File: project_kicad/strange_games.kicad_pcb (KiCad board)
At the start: 2 copper layers, 330 x 248.8 mm, 117 parts, among them J1 Display, M1 Motor_DC, Q1 Si2302A, Q3 Si2302A, Q4 Q_Photo, SW10 SW_Push, SW11 SW_Push, SW3 SW_Push, SW4 SW_Push, SW5 SW_Push, SW6 SW_Push, SW7 SW_Push, SW8 SW_Push, SW9 SW_Push, U1 charge controller, U2 boost converter, U3 LDL1117S33R, U4 ESP32-DEVKIT-V1, U5 TMP112xxDRL, U6 vibrating_sensor, U7 LSM6DS3, U8 MQ-135 gas sensor

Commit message: code changes
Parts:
- added C5: C_Generic, PCM_Capacitor_SMD_AKL:C_0402_1005Metric, F.Cu at (347.9, 47.6)
- added R19: 330_0805, PCM_4ms_Resistor:R_0805_2012Metric, F.Cu at (348.5, 42.1)
- added R27: 10k_0805, PCM_4ms_Resistor:R_0805_2012Metric, F.Cu at (348.5, 45.1)
- added SW1: SW_Push, Button_Switch_THT:SW_PUSH-12mm, F.Cu at (331.5, 44.9)
- added SW12: SW_Push, Button_Switch_THT:SW_PUSH-12mm, F.Cu at (331.5, 72.0)
- added SW2: SW_Push, Button_Switch_THT:SW_PUSH-12mm, F.Cu at (331.5, 58.5)

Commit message: pcb update
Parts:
- SW1, SW12, SW2: moved to B.Cu
- moved BT1 272.9 mm to (3.23, 10.3)
- moved SW1 184.7 mm to (146.8, 41.5), turned to -90 degrees
- moved C2 174.5 mm to (196.6, 50.6)
- moved Q4 174.5 mm to (203.2, 47.5)
- moved R20 174.5 mm to (200.6, 50.6)
- moved R28 174.5 mm to (198.6, 50.6)
- moved SW2 165.6 mm to (166.8, 41.5), turned to -90 degrees
- moved C5 160.3 mm to (187.6, 44.5), turned to 180 degrees
- moved R19 158.1 mm to (190.4, 44.5), turned to 180 degrees
- moved R27 158.1 mm to (190.4, 47.0)
- moved D3 151.9 mm to (155.2, 137.4), turned to 0 degrees
- moved SW12 147.9 mm to (186.8, 41.5), turned to -90 degrees
- moved L1 147.1 mm to (154.0, 141.2), turned to 90 degrees
- moved Q1 140.6 mm to (156.5, 145.3), turned to 90 degrees
- moved R15 140.1 mm to (153.1, 146.4), turned to 180 degrees
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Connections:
- J1 pad 23: SCL -> CLK
- U4 pad 12: B12 -> B8
- U4 pad 13: B6 -> B9
- U4 pad 17: B10 -> gas_signal
- U4 pad 18: B9 -> vibrating_signal
- U4 pad 19: open_box -> vibrating_motor
- U4 pad 20: vibrating_motor -> open_box
- U4 pad 21: B2 -> luminodiodes
- U4 pad 22: B1 -> B10
- U4 pad 23: B5 -> B11
- U4 pad 24: B4 -> B12
- U4 pad 25: B3 -> photo
- U4 pad 27: B11 -> A0_display
- U4 pad 3: A0_display -> B1
- U4 pad 4: luminodiodes -> B2
- U4 pad 5: vibrating_signal -> B3
- U4 pad 6: B8 -> B4
- U4 pad 7: B7 -> B5
- U4 pad 8: gas_signal -> B6
- U4 pad 9: photo -> B7
- U8 pad 3: gas_signal -> unconnected-(U8-AO-Pad3)
- U8 pad 4: unconnected-(U8-AO-Pad4) -> gas_signal
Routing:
- net vibrating_motor: track 0.00 -> 62.1 mm
- net open_box: track 0.00 -> 48.4 mm
- net VDC: track 32.1 -> 67.2 mm
- net A0_display: track 0.00 -> 33.7 mm, vias 0 -> 2
- net photo: track 4.12 -> 37.1 mm
- net B12: track 0.00 -> 32.8 mm
- net CLK: track 0.00 -> 32.1 mm, vias 0 -> 2
- net B11: track 0.00 -> 31.4 mm
- net MOSI: track 0.00 -> 29.5 mm
- net B10: track 0.00 -> 28.6 mm
- net vibrating_signal: track 2.87 -> 30.9 mm
- net GND: track 32.8 -> 53.5 mm, vias 20 -> 28
- net +12V: track 10.5 -> 30.5 mm
- net gas_signal: track 2.98 -> 19.8 mm
- net Net-(R4-Pad1): track 0.00 -> 12.5 mm
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- added copper zone on F.Cu, net +12V
- added copper zone on F.Cu, net VDC
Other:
- board size 330 x 248.8 mm -> 320 x 240 mm

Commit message: made pcb
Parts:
- removed BT1: Battery_Cell, Battery:BatteryHolder_MPD_BH-18650-PC2
- moved R29 20.8 mm to (185.4, 141.4)
- moved C36 20.8 mm to (186.1, 146.5)
- moved U6 20.8 mm to (189.2, 146.5)
- moved C2 12.8 mm to (188.7, 60.6)
- moved C5 12.8 mm to (179.6, 54.5)
- moved C6 12.8 mm to (139.6, 54.5)
- moved C7 12.8 mm to (159.6, 54.5)
- moved Q4 12.8 mm to (195.2, 57.5)
- moved R19 12.8 mm to (182.4, 54.5)
- moved R20 12.8 mm to (192.7, 60.6)
- moved R27 12.8 mm to (182.4, 57.0)
- moved R28 12.8 mm to (190.7, 60.6)
- moved R3 12.8 mm to (142.4, 54.5)
- moved R4 12.8 mm to (162.4, 54.5)
- moved R5 12.8 mm to (142.4, 57.0)
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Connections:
- net A0_display renamed A0
- net gas_signal renamed GasSensor
- net photo renamed PhotoSensor
- net vibrating_signal renamed VibrationSensor
- D5 pad 4: luminodiodes -> Luminodiodes
- R15 pad 2: open_box -> Door
- R17 pad 2: vibrating_motor -> VibrationMotor
- U4 pad 19: vibrating_motor -> Luminodiodes
- U4 pad 20: open_box -> VibrationMotor
- U4 pad 21: luminodiodes -> Door
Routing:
- net B10: track 28.6 -> 173.6 mm, vias 0 -> 2
- net B8: track 1.21 -> 138.8 mm, vias 0 -> 2
- net B11: track 31.4 -> 155.2 mm, vias 0 -> 2
- net B7: track 1.21 -> 122.8 mm, vias 0 -> 2
- net B9: track 1.21 -> 107.3 mm, vias 0 -> 2
- net B12: track 32.8 -> 134.3 mm, vias 0 -> 2
- net B4: track 1.21 -> 101.2 mm, vias 0 -> 2
- net B5: track 1.21 -> 82.2 mm, vias 0 -> 2
- net PhotoSensor: track 37.1 -> 108.9 mm, vias 0 -> 2
- net vibrating_motor: track 62.1 -> 0.00 mm
- net B6: track 1.21 -> 62.6 mm, vias 0 -> 2
- net VibrationMotor: track 0.00 -> 57.5 mm
- net Luminodiodes: track 0.00 -> 49.5 mm, vias 0 -> 2
- net open_box: track 48.4 -> 0.00 mm
- net B1: track 1.21 -> 48.2 mm, vias 0 -> 2
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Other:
- board size 320 x 240 mm -> 150 x 225 mm

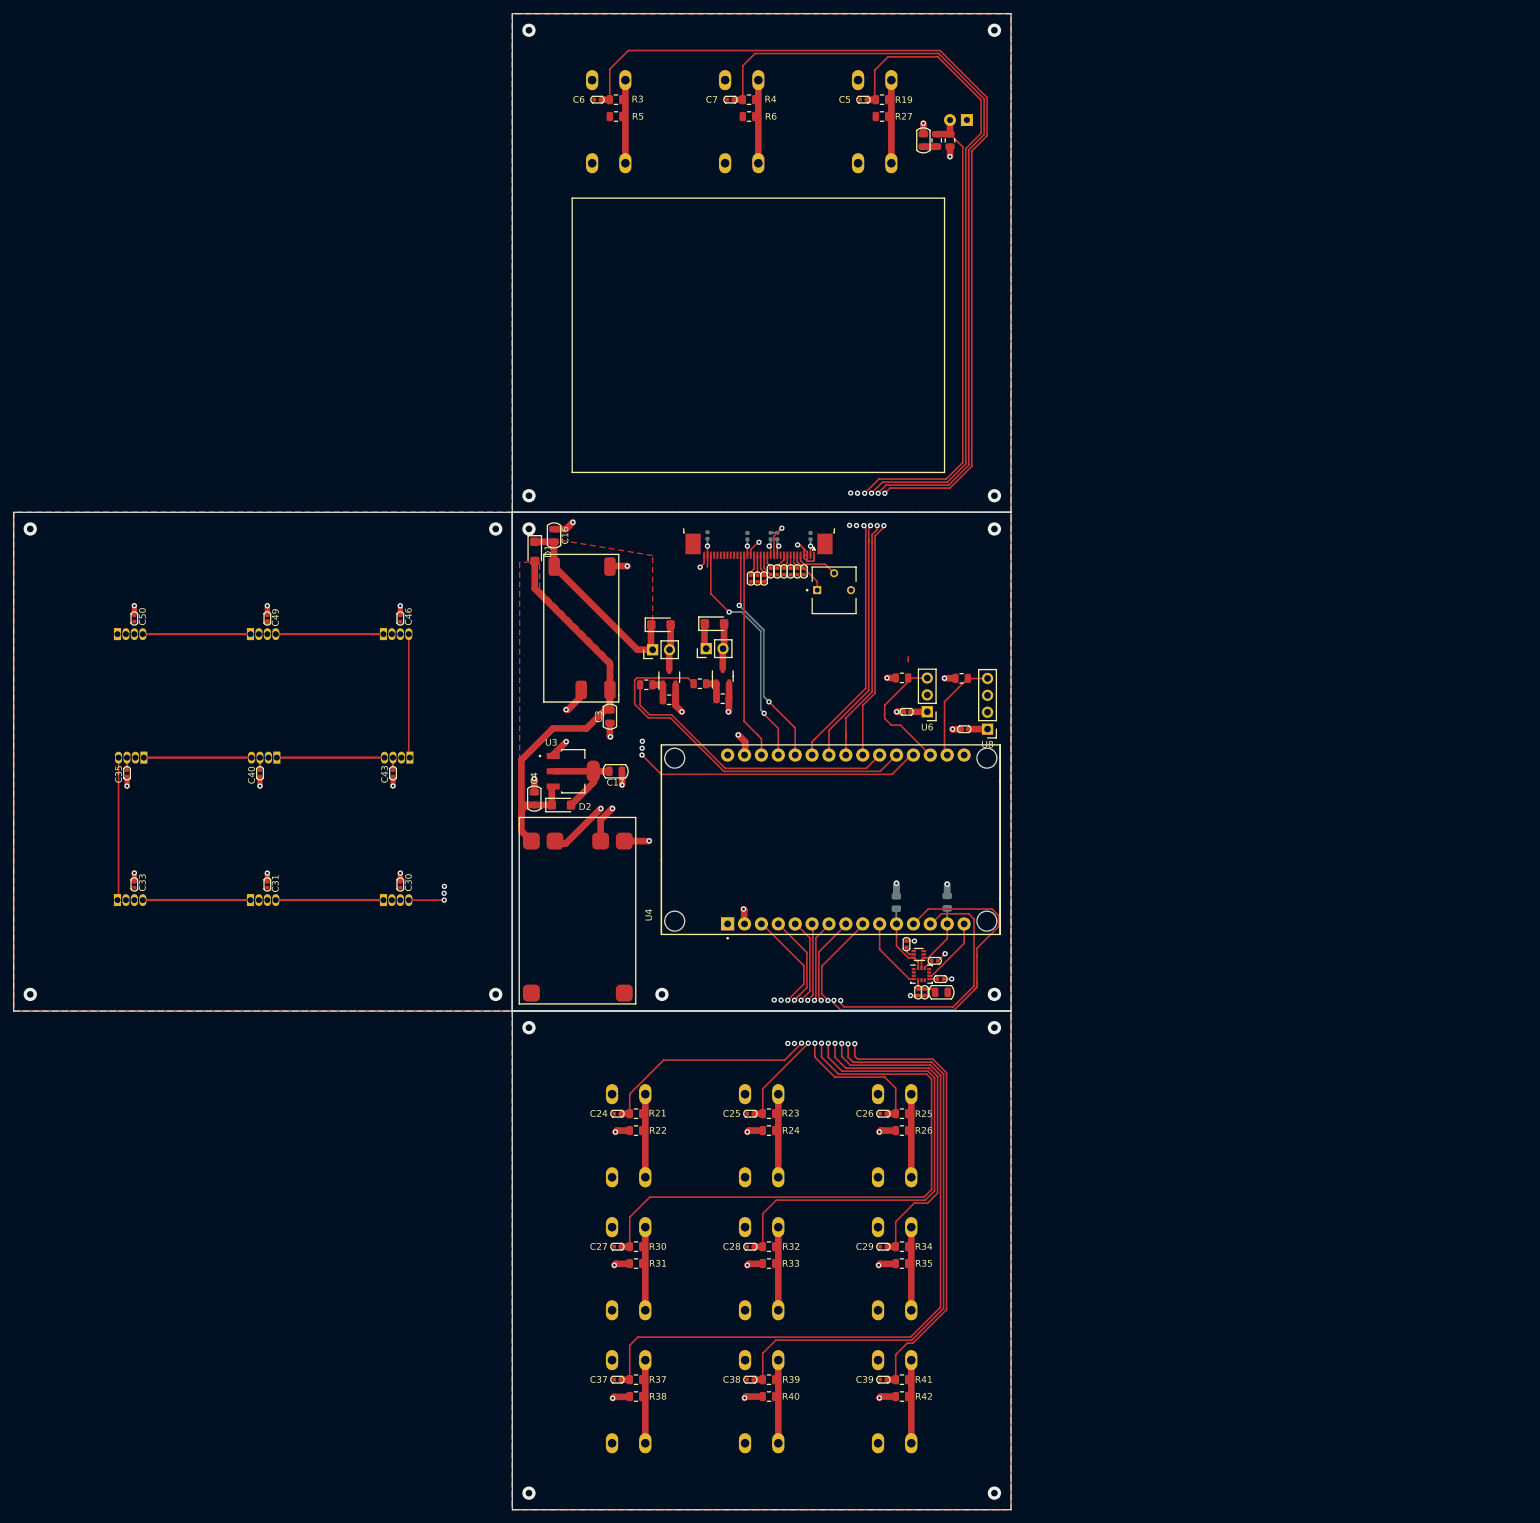
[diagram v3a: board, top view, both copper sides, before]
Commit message: code update and pcb remade a0 track
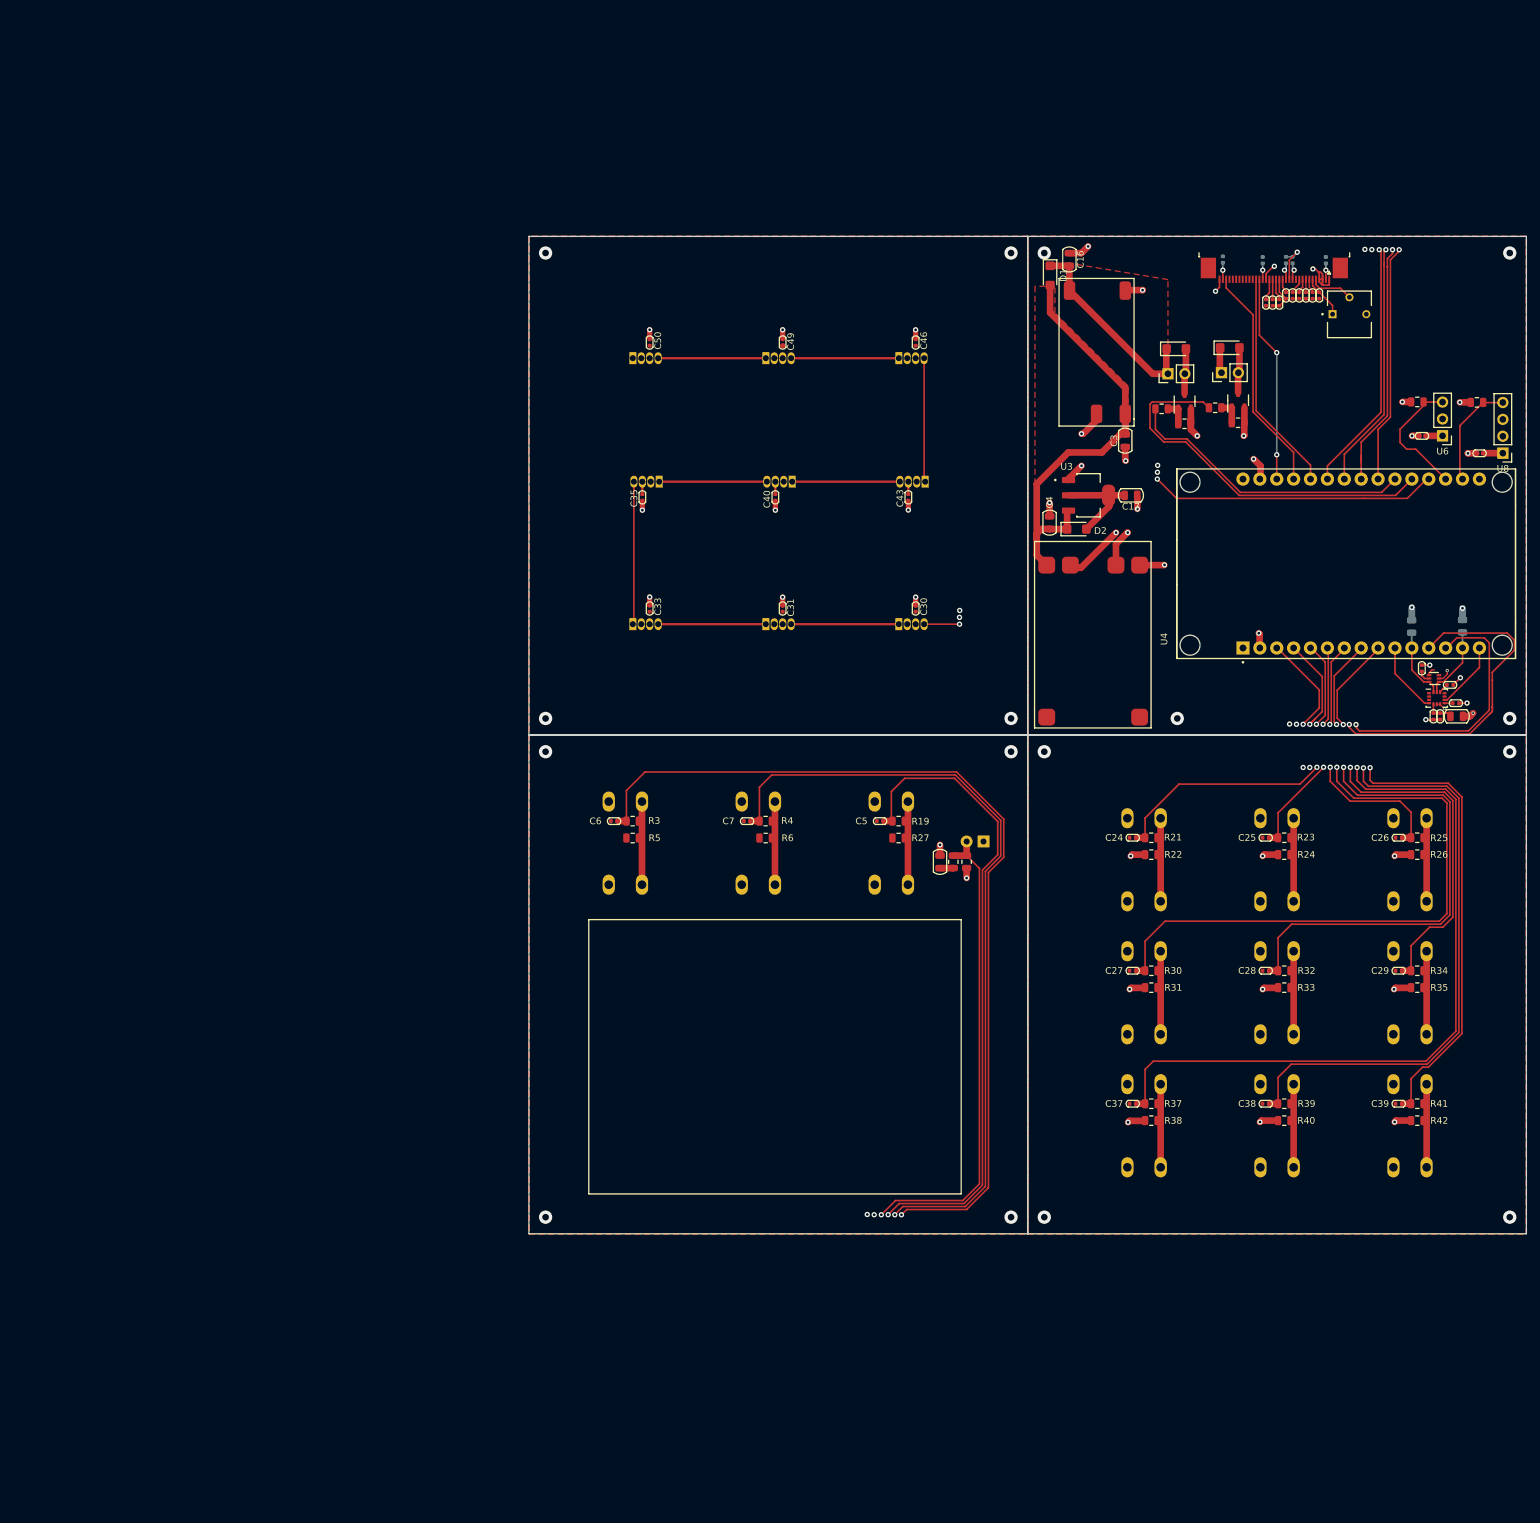
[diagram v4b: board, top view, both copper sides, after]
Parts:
- moved C2 108.5 mm to (191.2, 169.1)
- moved C5 108.5 mm to (182.1, 163.0)
- moved C6 108.5 mm to (142.1, 163.0)
- moved C7 108.5 mm to (162.1, 163.0)
- moved Q4 108.5 mm to (197.7, 166.0)
- moved R19 108.5 mm to (184.9, 163.0)
- moved R20 108.5 mm to (195.2, 169.1)
- moved R27 108.5 mm to (184.9, 165.5)
- moved R28 108.5 mm to (193.2, 169.1)
- moved R3 108.5 mm to (144.9, 163.0)
- moved R4 108.5 mm to (164.9, 163.0)
- moved R5 108.5 mm to (144.9, 165.5)
- moved R6 108.5 mm to (164.9, 165.5)
- moved SW1 108.5 mm to (141.3, 160.0)
- moved SW12 108.5 mm to (181.3, 160.0)
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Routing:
- net GND: track 93.2 -> 98.6 mm, vias 49 -> 52
- net A0: track 35.4 -> 34.3 mm, vias 2 -> 0
- net VibrationSensor: track 20.3 -> 19.6 mm
- net CLK: track 33.7 -> 33.4 mm, vias 2 -> 0
- net MOSI: vias 0 -> 2
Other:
- board size 150 x 225 mm -> 150 x 150 mm

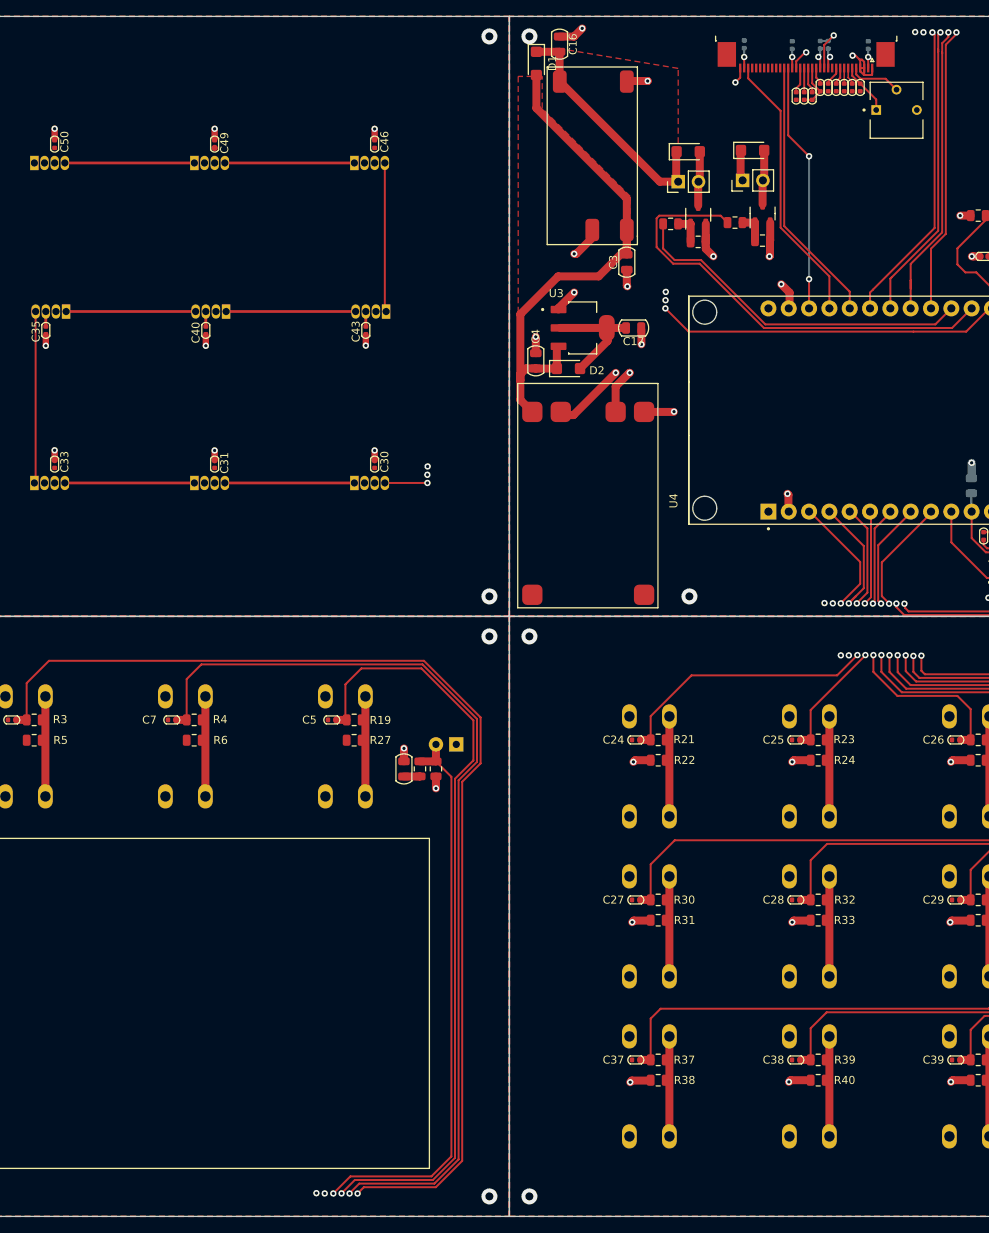
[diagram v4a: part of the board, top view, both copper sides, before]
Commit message: pcb changes deleted 1 button and made /res pin
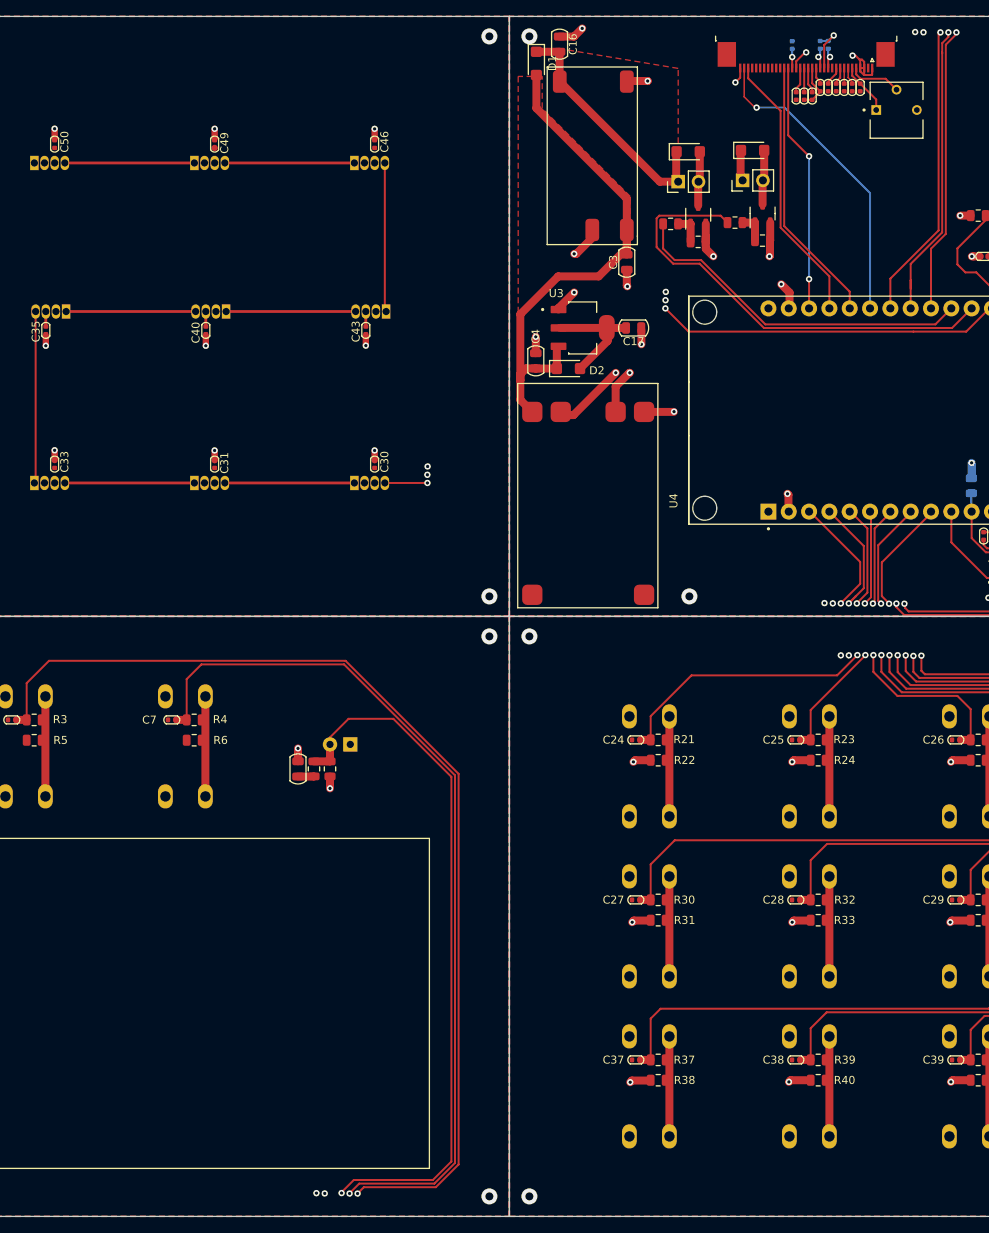
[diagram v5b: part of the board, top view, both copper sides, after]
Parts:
- removed C10, C45, C5: C_Generic, PCM_Capacitor_SMD_AKL:C_0402_1005Metric
- removed R19: 330_0805, PCM_4ms_Resistor:R_0805_2012Metric
- removed R27: 10k_0805, PCM_4ms_Resistor:R_0805_2012Metric
- removed SW12: SW_Push, Button_Switch_THT:SW_PUSH-12mm
- moved C2 13.2 mm to (177.9, 169.1)
- moved R20 13.2 mm to (181.9, 169.1)
- moved R28 13.2 mm to (179.9, 169.1)
- moved Q4 13.2 mm to (184.5, 166.0)
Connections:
- J1 pad 33: +3V3 -> /res
- U4 pad 24: B12 -> PhotoSensor
- U4 pad 25: PhotoSensor -> /res
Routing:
- net B12: track 134.3 -> 0.00 mm, vias 2 -> 0
- net /res: track 0.00 -> 38.7 mm, vias 0 -> 1
- net PhotoSensor: track 108.9 -> 124.7 mm
- net Net-(R19-Pad1): track 12.5 -> 0.00 mm
- net B10: track 173.6 -> 165.6 mm
- net B11: track 155.2 -> 147.2 mm
- net +3V3: track 50.9 -> 46.0 mm, vias 11 -> 9
